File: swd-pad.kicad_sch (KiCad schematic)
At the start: 5 parts, among them J6 OroConn6p

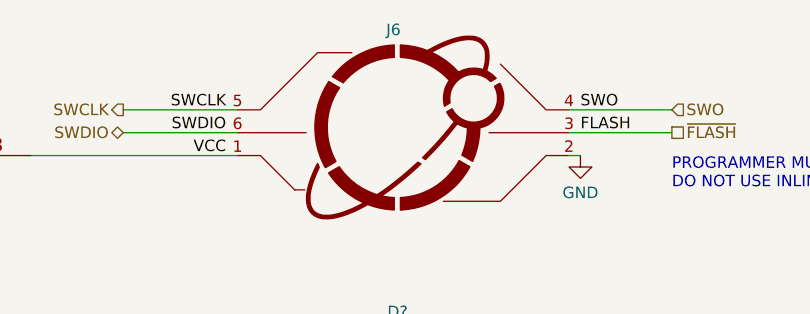
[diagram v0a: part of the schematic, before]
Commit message: first few boards laid out
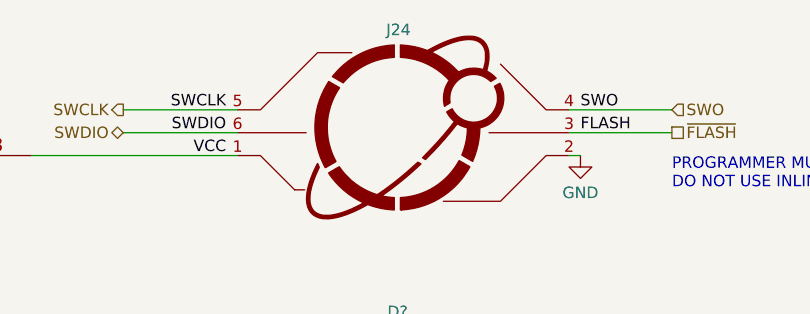
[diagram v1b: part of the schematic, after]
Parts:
- CR1: footprint DPAK3_TO-252_WEN -> BYV10D-600PJ:BYV10D-600PJ; Manufacturer_Name (none) -> WeEn Semiconductors; Manufacturer_Part_Number (none) -> BYV10D-600PJ; Mouser Part Number (none) -> 771-BYV10D-600PJ; Mouser Price/Stock (none) -> https://www.mouser.de/ProductDetail/WeEn-Semiconductors/BYV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
- renumbered J6 to J24
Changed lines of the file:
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@@
     (rev "2")
     (company "Oro Operating System")
+    (comment 1 "://oro.sh")
+    (comment 2 "Joshua Lee Junon")
   )
   (no_connect (at 166.37 115.57))
@@
         )
         (path "/e89dcd22-1250-4a5b-b778-1c95a0dd623d/259c9346-7ad9-40c3-9e14-9b19afc78ddf"
-          (reference "#PWR095") (unit 1)
+          (reference "#PWR0131") (unit 1)
         )
       )
@@
         )
         (path "/e89dcd22-1250-4a5b-b778-1c95a0dd623d/259c9346-7ad9-40c3-9e14-9b19afc78ddf"
-          (reference "D10") (unit 1)
+          (reference "D8") (unit 1)
         )
       )
@@
         )
         (path "/e89dcd22-1250-4a5b-b778-1c95a0dd623d/259c9346-7ad9-40c3-9e14-9b19afc78ddf"
-          (reference "D11") (unit 1)
+          (reference "D9") (unit 1)
         )
       )
@@
         )
         (path "/e89dcd22-1250-4a5b-b778-1c95a0dd623d/259c9346-7ad9-40c3-9e14-9b19afc78ddf"
-          (reference "#PWR090") (unit 1)
+          (reference "#PWR0126") (unit 1)
         )
       )
@@
         )
         (path "/e89dcd22-1250-4a5b-b778-1c95a0dd623d/259c9346-7ad9-40c3-9e14-9b19afc78ddf"
-          (reference "#PWR093") (unit 1)
+          (reference "#PWR0129") (unit 1)
         )
       )
@@
   (symbol (lib_id "power:+3V3") (at 74.93 80.01 0) (unit 1)
     (in_bom yes) (on_board yes) (dnp no) (fields_autoplaced)
-    (property "Reference" "#PWR089" (at 74.93 83.82 0)
+    (property "Reference" "#PWR0125" (at 74.93 83.82 0)
       (effects (font (size 1.27 1.27)) hide)
     )
@@
       (project "Oro Link rev2"
         (path "/e89dcd22-1250-4a5b-b778-1c95a0dd623d/259c9346-7ad9-40c3-9e14-9b19afc78ddf"
-          (reference "#PWR089") (unit 1)
+          (reference "#PWR0125") (unit 1)
         )
       )
@@
   (symbol (lib_id "Oro:OroConn6p") (at 149.86 78.74 0) (unit 1)
     (in_bom no) (on_board yes) (dnp no)
-    (property "Reference" "J6" (at 148.59 68.58 0)
+    (property "Reference" "J24" (at 148.59 68.58 0)
       (effects (font (size 1.27 1.27)) (justify left))
     )
@@
       (project "Oro Link rev2"
         (path "/e89dcd22-1250-4a5b-b778-1c95a0dd623d/259c9346-7ad9-40c3-9e14-9b19afc78ddf"
-          (reference "J6") (unit 1)
+          (reference "J24") (unit 1)
         )
       )
@@
   (symbol (lib_id "power:GND") (at 170.18 82.55 0) (unit 1)
     (in_bom yes) (on_board yes) (dnp no) (fields_autoplaced)
-    (property "Reference" "#PWR094" (at 170.18 88.9 0)
+    (property "Reference" "#PWR0130" (at 170.18 88.9 0)
       (effects (font (size 1.27 1.27)) hide)
     )
@@
       (project "Oro Link rev2"
         (path "/e89dcd22-1250-4a5b-b778-1c95a0dd623d/259c9346-7ad9-40c3-9e14-9b19afc78ddf"
-          (reference "#PWR094") (unit 1)
+          (reference "#PWR0130") (unit 1)
         )
       )
@@
         )
         (path "/e89dcd22-1250-4a5b-b778-1c95a0dd623d/259c9346-7ad9-40c3-9e14-9b19afc78ddf"
-          (reference "#PWR092") (unit 1)
+          (reference "#PWR0128") (unit 1)
         )
       )
@@
         )
         (path "/e89dcd22-1250-4a5b-b778-1c95a0dd623d/259c9346-7ad9-40c3-9e14-9b19afc78ddf"
-          (reference "#PWR091") (unit 1)
+          (reference "#PWR0127") (unit 1)
         )
       )
@@
       (effects (font (size 1.524 1.524)))
     )
-    (property "Footprint" "DPAK3_TO-252_WEN" (at 96.52 76.454 0)
+    (property "Footprint" "BYV10D-600PJ:BYV10D-600PJ" (at 96.52 76.454 0)
       (effects (font (size 1.524 1.524)) hide)
     )
-    (property "Datasheet" "" (at 83.82 80.01 0)
-      (effects (font (size 1.524 1.524)))
+    (property "Datasheet" "https://www.mouser.de/datasheet/2/848/BYV10D_600P-1947876.pdf" (at 83.82 80.01 0)
+      (effects (font (size 1.524 1.524)) hide)
+    )
+    (property "Manufacturer_Name" "WeEn Semiconductors" (at 83.82 80.01 0)
+      (effects (font (size 1.27 1.27)) (justify left) hide)
+    )
+    (property "Manufacturer_Part_Number" "BYV10D-600PJ" (at 83.82 80.01 0)
+      (effects (font (size 1.27 1.27)) (justify left) hide)
+    )
+    (property "Mouser Part Number" "771-BYV10D-600PJ" (at 83.82 80.01 0)
+      (effects (font (size 1.27 1.27)) (justify left) hide)
+    )
+    (property "Mouser Price/Stock" "https://www.mouser.de/ProductDetail/WeEn-Semiconductors/BYV10D-600PJ" (at 83.82 80.01 0)
+      (effects (font (size 1.27 1.27)) (justify left) hide)
     )
     (pin "1")
@@
         )
         (path "/e89dcd22-1250-4a5b-b778-1c95a0dd623d/259c9346-7ad9-40c3-9e14-9b19afc78ddf"
-          (reference "C51") (unit 1)
-        )
-      )
+          (reference "C52") (unit 1)
+        )
+      )

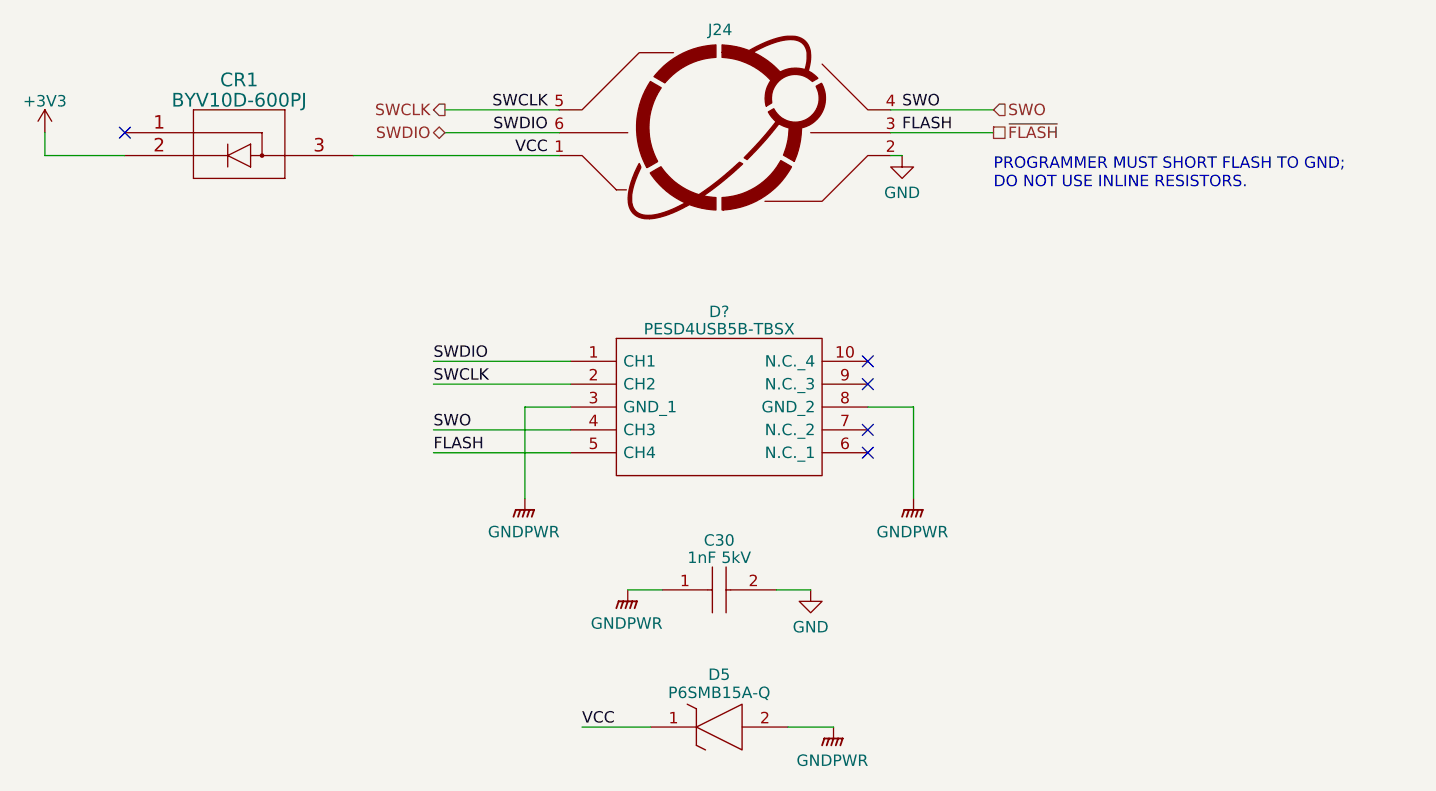
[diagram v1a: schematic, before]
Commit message: first panelization of entire modular dev board
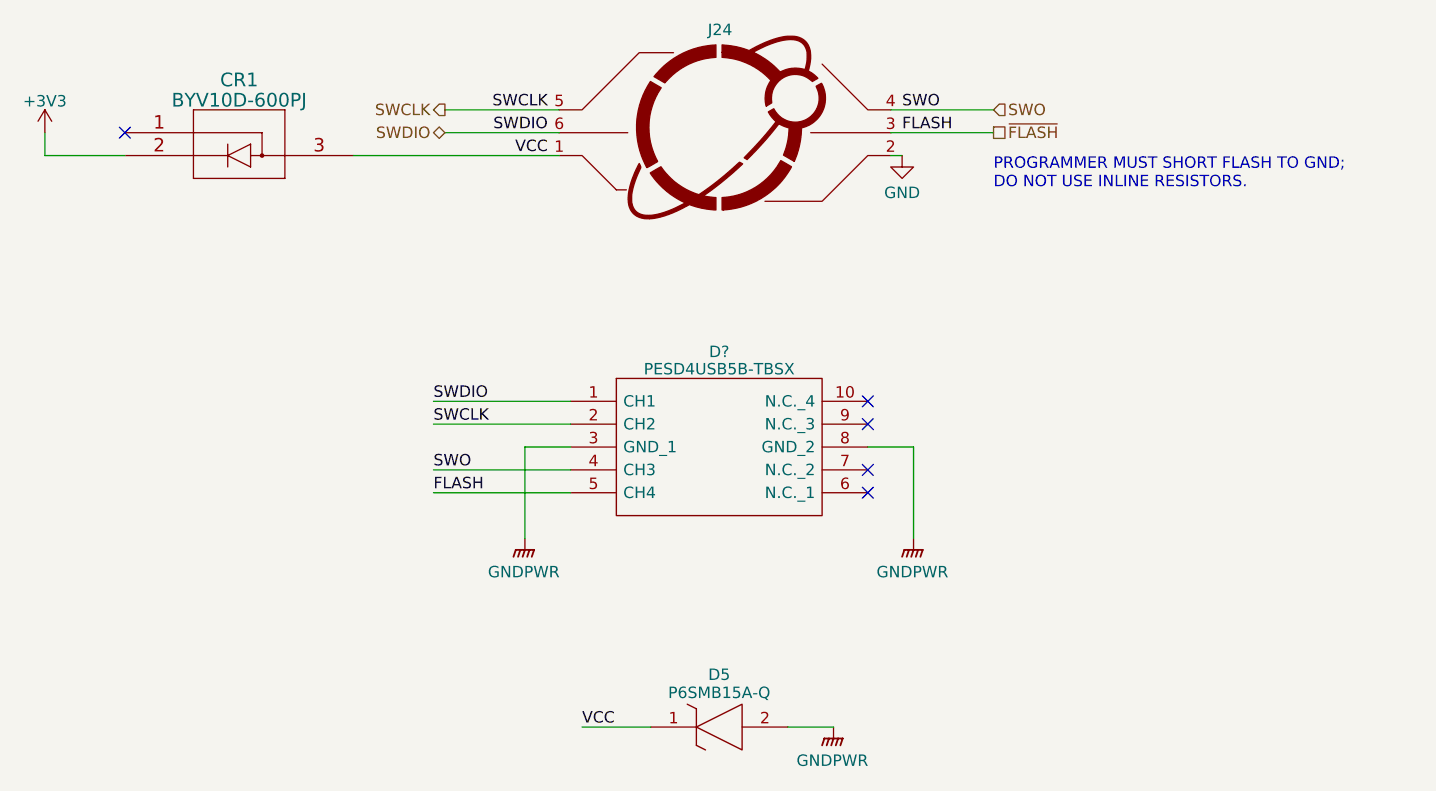
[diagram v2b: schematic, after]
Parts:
- removed C30: 1nF 5kV, CAPC5664X270N, symbol SamacSys_Parts:HV2225Y102KXMATHV
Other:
- moved on the sheet: D?

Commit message: initial board layout
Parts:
- renumbered J24 to J6
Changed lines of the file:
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@@
         )
         (path "/e89dcd22-1250-4a5b-b778-1c95a0dd623d/259c9346-7ad9-40c3-9e14-9b19afc78ddf"
-          (reference "#PWR0131") (unit 1)
+          (reference "#PWR076") (unit 1)
         )
       )
@@
         )
         (path "/e89dcd22-1250-4a5b-b778-1c95a0dd623d/259c9346-7ad9-40c3-9e14-9b19afc78ddf"
-          (reference "D8") (unit 1)
+          (reference "D7") (unit 1)
         )
       )
@@
         )
         (path "/e89dcd22-1250-4a5b-b778-1c95a0dd623d/259c9346-7ad9-40c3-9e14-9b19afc78ddf"
-          (reference "D9") (unit 1)
+          (reference "D8") (unit 1)
         )
       )
@@
         )
         (path "/e89dcd22-1250-4a5b-b778-1c95a0dd623d/259c9346-7ad9-40c3-9e14-9b19afc78ddf"
-          (reference "#PWR0126") (unit 1)
+          (reference "#PWR073") (unit 1)
         )
       )
@@
         )
         (path "/e89dcd22-1250-4a5b-b778-1c95a0dd623d/259c9346-7ad9-40c3-9e14-9b19afc78ddf"
-          (reference "#PWR0129") (unit 1)
+          (reference "#PWR074") (unit 1)
         )
       )
@@
   (symbol (lib_id "power:+3V3") (at 74.93 80.01 0) (unit 1)
     (in_bom yes) (on_board yes) (dnp no) (fields_autoplaced)
-    (property "Reference" "#PWR0125" (at 74.93 83.82 0)
+    (property "Reference" "#PWR072" (at 74.93 83.82 0)
       (effects (font (size 1.27 1.27)) hide)
     )
@@
       (project "Oro Link rev2"
         (path "/e89dcd22-1250-4a5b-b778-1c95a0dd623d/259c9346-7ad9-40c3-9e14-9b19afc78ddf"
-          (reference "#PWR0125") (unit 1)
+          (reference "#PWR072") (unit 1)
         )
       )
@@
   (symbol (lib_id "Oro:OroConn6p") (at 149.86 78.74 0) (unit 1)
     (in_bom no) (on_board yes) (dnp no)
-    (property "Reference" "J24" (at 148.59 68.58 0)
+    (property "Reference" "J6" (at 148.59 68.58 0)
       (effects (font (size 1.27 1.27)) (justify left))
     )
@@
       (project "Oro Link rev2"
         (path "/e89dcd22-1250-4a5b-b778-1c95a0dd623d/259c9346-7ad9-40c3-9e14-9b19afc78ddf"
-          (reference "J24") (unit 1)
+          (reference "J6") (unit 1)
         )
       )
@@
   (symbol (lib_id "power:GND") (at 170.18 82.55 0) (unit 1)
     (in_bom yes) (on_board yes) (dnp no) (fields_autoplaced)
-    (property "Reference" "#PWR0130" (at 170.18 88.9 0)
+    (property "Reference" "#PWR075" (at 170.18 88.9 0)
       (effects (font (size 1.27 1.27)) hide)
     )
@@
       (project "Oro Link rev2"
         (path "/e89dcd22-1250-4a5b-b778-1c95a0dd623d/259c9346-7ad9-40c3-9e14-9b19afc78ddf"
-          (reference "#PWR0130") (unit 1)
-        )
-      )
+          (reference "#PWR075") (unit 1)
+        )
+      )

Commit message: improve ESD, net classes and power diodes
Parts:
- removed CR1: BYV10D-600PJ, BYV10D-600PJ:BYV10D-600PJ, symbol 2023-03-11_13-46-16:BYV10D-600PJ
- added D15: RFU02VSM8STR, SODFL2514X80N, symbol SamacSys_Parts:RFU02VSM8STR
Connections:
- net VCC: now also D15.2
- new net +5V: D15.1
- no-connect marks 5 -> 4
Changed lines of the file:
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@@
   )
   (no_connect (at 166.37 120.015))
-  (no_connect (at 83.82 80.01))
   (no_connect (at 166.37 109.855))
   (no_connect (at 166.37 112.395))
@@
     (stroke (width 0) (type default))
   )
-  (wire (pts (xy 109.22 82.55) (xy 132.08 82.55))
-    (stroke (width 0) (type default))
-  )
-  (wire (pts (xy 74.93 80.01) (xy 74.93 82.55))
+  (wire (pts (xy 107.95 82.55) (xy 132.08 82.55))
     (stroke (width 0) (type default))
   )
@@
     (stroke (width 0) (type default))
   )
-  (wire (pts (xy 83.82 82.55) (xy 74.93 82.55))
+  (wire (pts (xy 86.995 82.55) (xy 92.71 82.55))
     (stroke (width 0) (type default))
   )
@@
         )
         (path "/e89dcd22-1250-4a5b-b778-1c95a0dd623d/259c9346-7ad9-40c3-9e14-9b19afc78ddf"
-          (reference "#PWR076") (unit 1)
+          (reference "#PWR073") (unit 1)
         )
       )
@@
         )
         (path "/e89dcd22-1250-4a5b-b778-1c95a0dd623d/259c9346-7ad9-40c3-9e14-9b19afc78ddf"
-          (reference "D7") (unit 1)
+          (reference "D11") (unit 1)
         )
       )
@@
         )
         (path "/e89dcd22-1250-4a5b-b778-1c95a0dd623d/259c9346-7ad9-40c3-9e14-9b19afc78ddf"
-          (reference "D8") (unit 1)
+          (reference "D12") (unit 1)
         )
       )
@@
         )
         (path "/e89dcd22-1250-4a5b-b778-1c95a0dd623d/259c9346-7ad9-40c3-9e14-9b19afc78ddf"
-          (reference "#PWR073") (unit 1)
+          (reference "#PWR070") (unit 1)
         )
       )
@@
         )
         (path "/e89dcd22-1250-4a5b-b778-1c95a0dd623d/259c9346-7ad9-40c3-9e14-9b19afc78ddf"
-          (reference "#PWR074") (unit 1)
-        )
-      )
-    )
-  )
-  (symbol (lib_id "power:+3V3") (at 74.93 80.01 0) (unit 1)
-    (in_bom yes) (on_board yes) (dnp no) (fields_autoplaced)
-    (property "Reference" "#PWR072" (at 74.93 83.82 0)
-      (effects (font (size 1.27 1.27)) hide)
-    )
-    (property "Value" "+3V3" (at 74.93 76.5081 0)
-      (effects (font (size 1.27 1.27)))
-    )
-    (property "Footprint" "" (at 74.93 80.01 0)
-      (effects (font (size 1.27 1.27)) hide)
-    )
-    (property "Datasheet" "" (at 74.93 80.01 0)
-      (effects (font (size 1.27 1.27)) hide)
-    )
-    (pin "1")
-    (instances
-      (project "Oro Link rev2"
-        (path "/e89dcd22-1250-4a5b-b778-1c95a0dd623d/259c9346-7ad9-40c3-9e14-9b19afc78ddf"
-          (reference "#PWR072") (unit 1)
+          (reference "#PWR071") (unit 1)
         )
       )
@@
   (symbol (lib_id "power:GND") (at 170.18 82.55 0) (unit 1)
     (in_bom yes) (on_board yes) (dnp no) (fields_autoplaced)
-    (property "Reference" "#PWR075" (at 170.18 88.9 0)
+    (property "Reference" "#PWR072" (at 170.18 88.9 0)
       (effects (font (size 1.27 1.27)) hide)
     )
@@
       (project "Oro Link rev2"
         (path "/e89dcd22-1250-4a5b-b778-1c95a0dd623d/259c9346-7ad9-40c3-9e14-9b19afc78ddf"
-          (reference "#PWR075") (unit 1)
-        )
-      )
-    )
-  )
-  (symbol (lib_id "2023-03-11_13-46-16:BYV10D-600PJ") (at 83.82 80.01 0) (unit 1)
-    (in_bom yes) (on_board yes) (dnp no) (fields_autoplaced)
-    (property "Reference" "CR1" (at 96.52 74.1504 0)
-      (effects (font (size 1.524 1.524)))
-    )
-    (property "Value" "BYV10D-600PJ" (at 96.52 76.4046 0)
-      (effects (font (size 1.524 1.524)))
-    )
-    (property "Footprint" "BYV10D-600PJ:BYV10D-600PJ" (at 96.52 76.454 0)
-      (effects (font (size 1.524 1.524)) hide)
-    )
-    (property "Datasheet" "https://www.mouser.de/datasheet/2/848/BYV10D_600P-1947876.pdf" (at 83.82 80.01 0)
-      (effects (font (size 1.524 1.524)) hide)
-    )
-    (property "Manufacturer_Name" "WeEn Semiconductors" (at 83.82 80.01 0)
-      (effects (font (size 1.27 1.27)) (justify left) hide)
-    )
-    (property "Manufacturer_Part_Number" "BYV10D-600PJ" (at 83.82 80.01 0)
-      (effects (font (size 1.27 1.27)) (justify left) hide)
-    )
-    (property "Mouser Part Number" "771-BYV10D-600PJ" (at 83.82 80.01 0)
-      (effects (font (size 1.27 1.27)) (justify left) hide)
-    )
-    (property "Mouser Price/Stock" "https://www.mouser.de/ProductDetail/WeEn-Semiconductors/BYV10D-600PJ" (at 83.82 80.01 0)
+          (reference "#PWR072") (unit 1)
+        )
+      )
+    )
+  )
+  (symbol (lib_id "power:+5V") (at 86.995 82.55 0) (unit 1)
+    (in_bom yes) (on_board yes) (dnp no) (fields_autoplaced)
+    (property "Reference" "#PWR069" (at 86.995 86.36 0)
+      (effects (font (size 1.27 1.27)) hide)
+    )
+    (property "Value" "+5V" (at 86.995 79.0481 0)
+      (effects (font (size 1.27 1.27)))
+    )
+    (property "Footprint" "" (at 86.995 82.55 0)
+      (effects (font (size 1.27 1.27)) hide)
+    )
+    (property "Datasheet" "" (at 86.995 82.55 0)
+      (effects (font (size 1.27 1.27)) hide)
+    )
+    (pin "1")
+    (instances
+      (project "Oro Link rev2"
+        (path "/e89dcd22-1250-4a5b-b778-1c95a0dd623d/259c9346-7ad9-40c3-9e14-9b19afc78ddf"
+          (reference "#PWR069") (unit 1)
+        )
+      )
+    )
+  )
+  (symbol (lib_id "SamacSys_Parts:RFU02VSM8STR") (at 92.71 82.55 0) (unit 1)
+    (in_bom yes) (on_board yes) (dnp no)
+    (property "Reference" "D15" (at 100.33 76.835 0)
+      (effects (font (size 1.27 1.27)))
+    )
+    (property "Value" "RFU02VSM8STR" (at 100.33 78.74 0)
+      (effects (font (size 1.27 1.27)))
+    )
+    (property "Footprint" "SODFL2514X80N" (at 104.14 82.55 0)
+      (effects (font (size 1.27 1.27)) (justify left) hide)
+    )
+    (property "Datasheet" "https://componentsearchengine.com/Datasheets/1/RFU02VSM8STR.pdf" (at 104.14 85.09 0)
+      (effects (font (size 1.27 1.27)) (justify left) hide)
+    )
+    (property "Description" "ROHM 800V 200mA, Diode, 2-Pin TUMD2M RFU02VSM8STR" (at 104.14 87.63 0)
+      (effects (font (size 1.27 1.27)) (justify left) hide)
+    )
+    (property "Height" "0.8" (at 104.14 90.17 0)
+      (effects (font (size 1.27 1.27)) (justify left) hide)
+    )
+    (property "Manufacturer_Name" "ROHM Semiconductor" (at 104.14 92.71 0)
+      (effects (font (size 1.27 1.27)) (justify left) hide)
+    )
+    (property "Manufacturer_Part_Number" "RFU02VSM8STR" (at 104.14 95.25 0)
+      (effects (font (size 1.27 1.27)) (justify left) hide)
+    )
+    (property "Mouser Part Number" "755-RFU02VSM8STR" (at 104.14 97.79 0)
+      (effects (font (size 1.27 1.27)) (justify left) hide)
+    )
+    (property "Mouser Price/Stock" "https://www.mouser.co.uk/ProductDetail/ROHM-Semiconductor/RFU02VSM8STR?qs=R91Bf2XdLdmknCjulGI%252B1w%3D%3D" (at 104.14 100.33 0)
+      (effects (font (size 1.27 1.27)) (justify left) hide)
+    )
+    (property "Arrow Part Number" "RFU02VSM8STR" (at 104.14 102.87 0)
+      (effects (font (size 1.27 1.27)) (justify left) hide)
+    )
+    (property "Arrow Price/Stock" "https://www.arrow.com/en/products/rfu02vsm8str/rohm-semiconductor" (at 104.14 105.41 0)
       (effects (font (size 1.27 1.27)) (justify left) hide)
     )
     (pin "1")
     (pin "2")
-    (pin "3")
-    (instances
-      (project "Oro Link rev2"
-        (path "/e89dcd22-1250-4a5b-b778-1c95a0dd623d/259c9346-7ad9-40c3-9e14-9b19afc78ddf"
-          (reference "CR1") (unit 1)
-        )
-      )
+    (instances
+      (project "Oro Link rev2"
+        (path "/e89dcd22-1250-4a5b-b778-1c95a0dd623d/259c9346-7ad9-40c3-9e14-9b19afc78ddf"
+          (reference "D15") (unit 1)
+        )
+      )
